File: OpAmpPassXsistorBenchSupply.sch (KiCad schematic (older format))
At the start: 32 parts

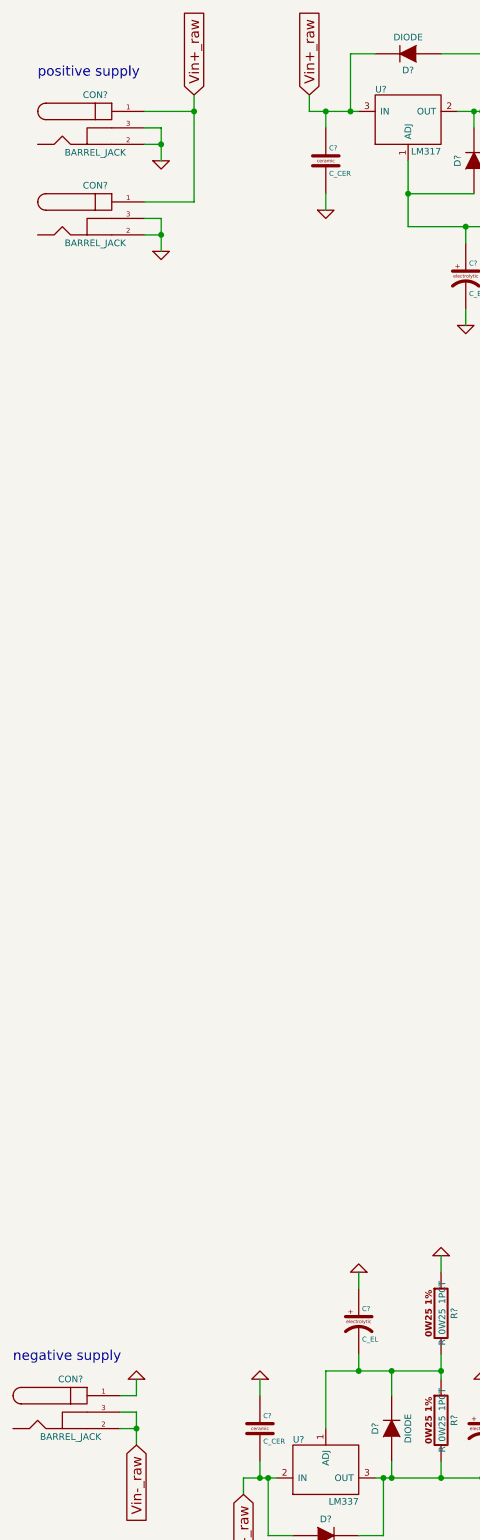
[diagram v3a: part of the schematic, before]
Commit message: adding input caps
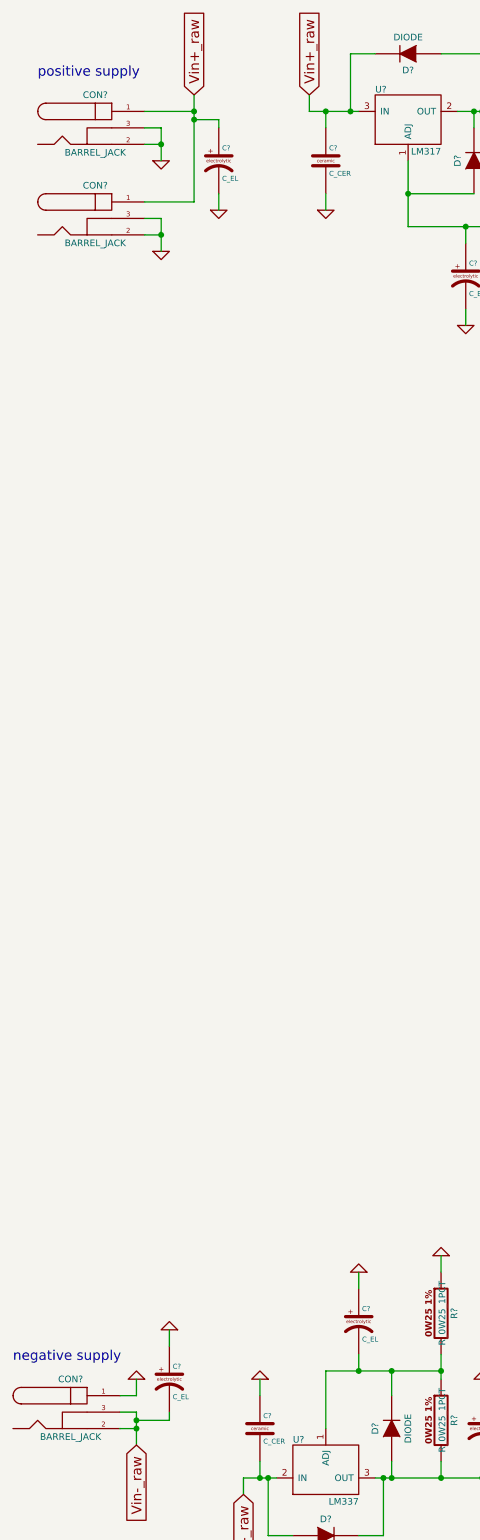
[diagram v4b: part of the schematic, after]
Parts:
- added C? (x2): C_EL, ~, symbol C_EL
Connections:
- net GND: now also C?.1, C?.2
- net Vin+_raw: now also C?.1
- net Vin-_raw: now also C?.2
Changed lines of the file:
@@
 Wire Wire Line
 	9750 8000 9950 8000
+$Comp
+L C_EL C?
+U 1 1 53366AD7
+P 2050 1700
+F 0 "C?" H 2070 1760 30  0000 L BNN
+F 1 "C_EL" H 2070 1610 30  0000 L TNN
+F 2 "~" H 2088 1550 30  0000 C CNN
+F 3 "~" H 2050 1700 60  0000 C CNN
+	1    2050 1700
+	1    0    0    -1
+$EndComp
+Wire Wire Line
+	1900 1450 2050 1450
+Wire Wire Line
+	2050 1450 2050 1500
+Connection ~ 1900 1450
+$Comp
+L GND #PWR?
+U 1 1 53366B79
+P 2050 2000
+F 0 "#PWR?" H 2050 2000 30  0001 C CNN
+F 1 "GND" H 2050 1930 30  0001 C CNN
+F 2 "" H 2050 2000 60  0000 C CNN
+F 3 "" H 2050 2000 60  0000 C CNN
+	1    2050 2000
+	1    0    0    -1
+$EndComp
+Wire Wire Line
+	2050 1900 2050 2000
+$Comp
+L C_EL C?
+U 1 1 53366C10
+P 1750 9100
+F 0 "C?" H 1770 9160 30  0000 L BNN
+F 1 "C_EL" H 1770 9010 30  0000 L TNN
+F 2 "~" H 1788 8950 30  0000 C CNN
+F 3 "~" H 1750 9100 60  0000 C CNN
+	1    1750 9100
+	1    0    0    -1
+$EndComp
+Wire Wire Line
+	1550 9350 1750 9350
+Wire Wire Line
+	1750 9350 1750 9300
+Connection ~ 1550 9350
+$Comp
+L GND #PWR?
+U 1 1 53366CB2
+P 1750 8800
+F 0 "#PWR?" H 1750 8800 30  0001 C CNN
+F 1 "GND" H 1750 8730 30  0001 C CNN
+F 2 "" H 1750 8800 60  0000 C CNN
+F 3 "" H 1750 8800 60  0000 C CNN
+	1    1750 8800
+	-1   0    0    1
+$EndComp
+Wire Wire Line
+	1750 8900 1750 8800
 $EndSCHEMATC

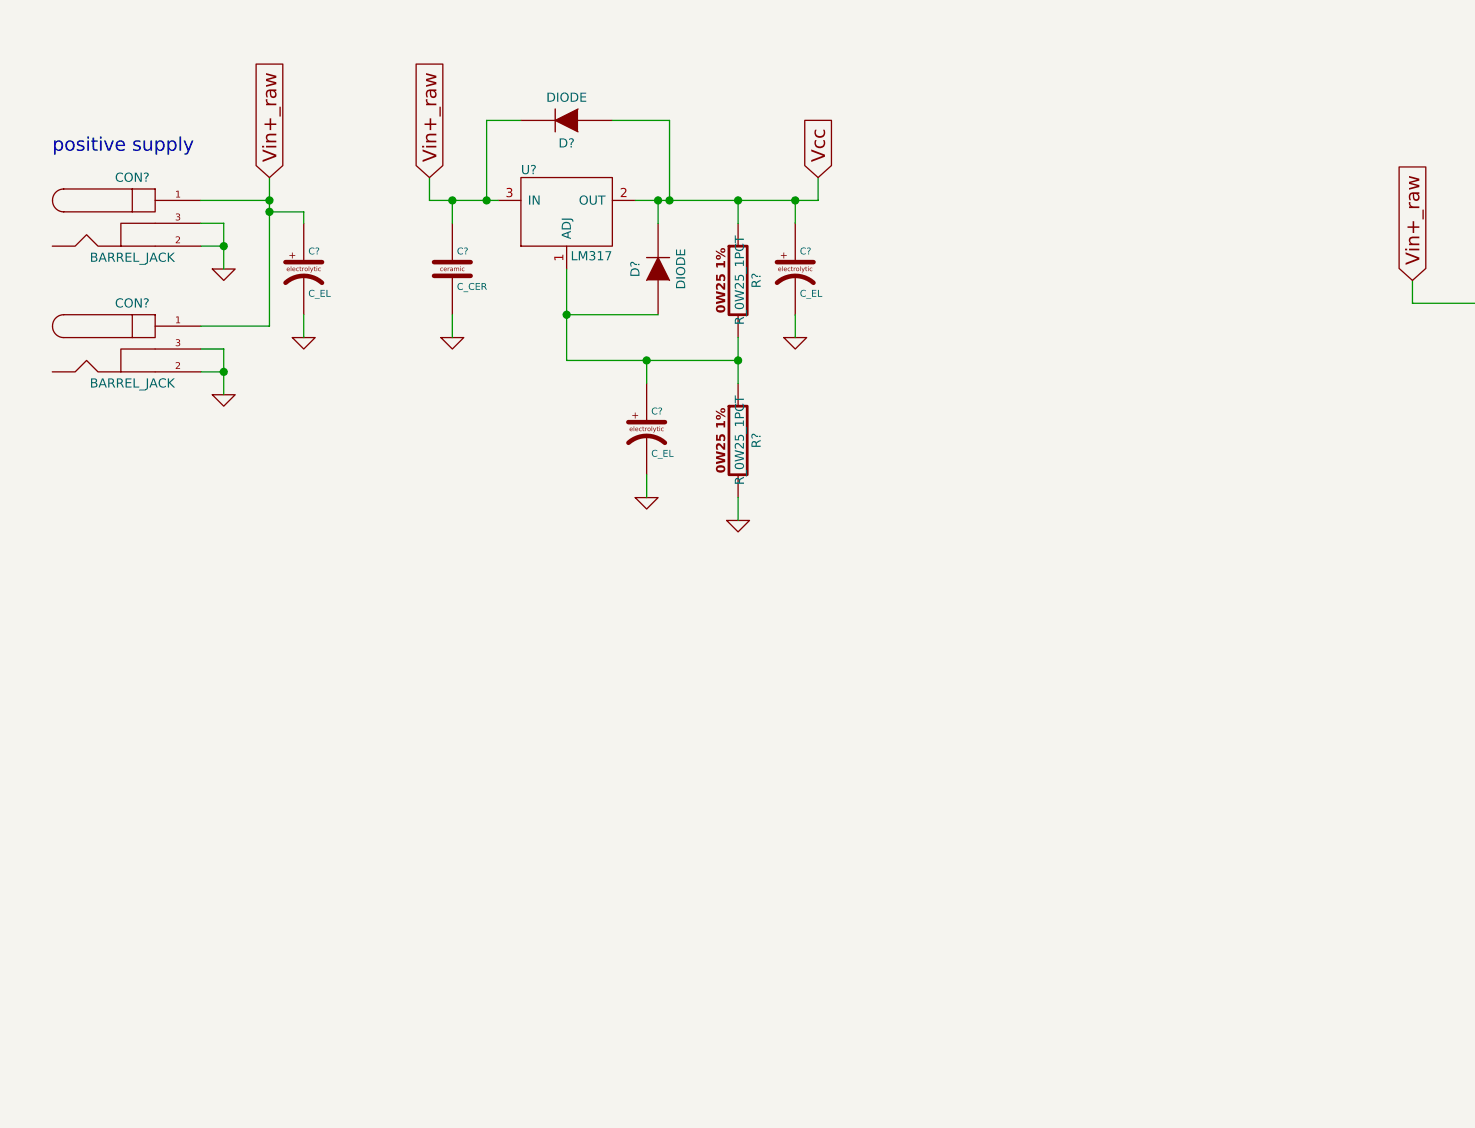
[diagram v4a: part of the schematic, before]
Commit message: adding input filter
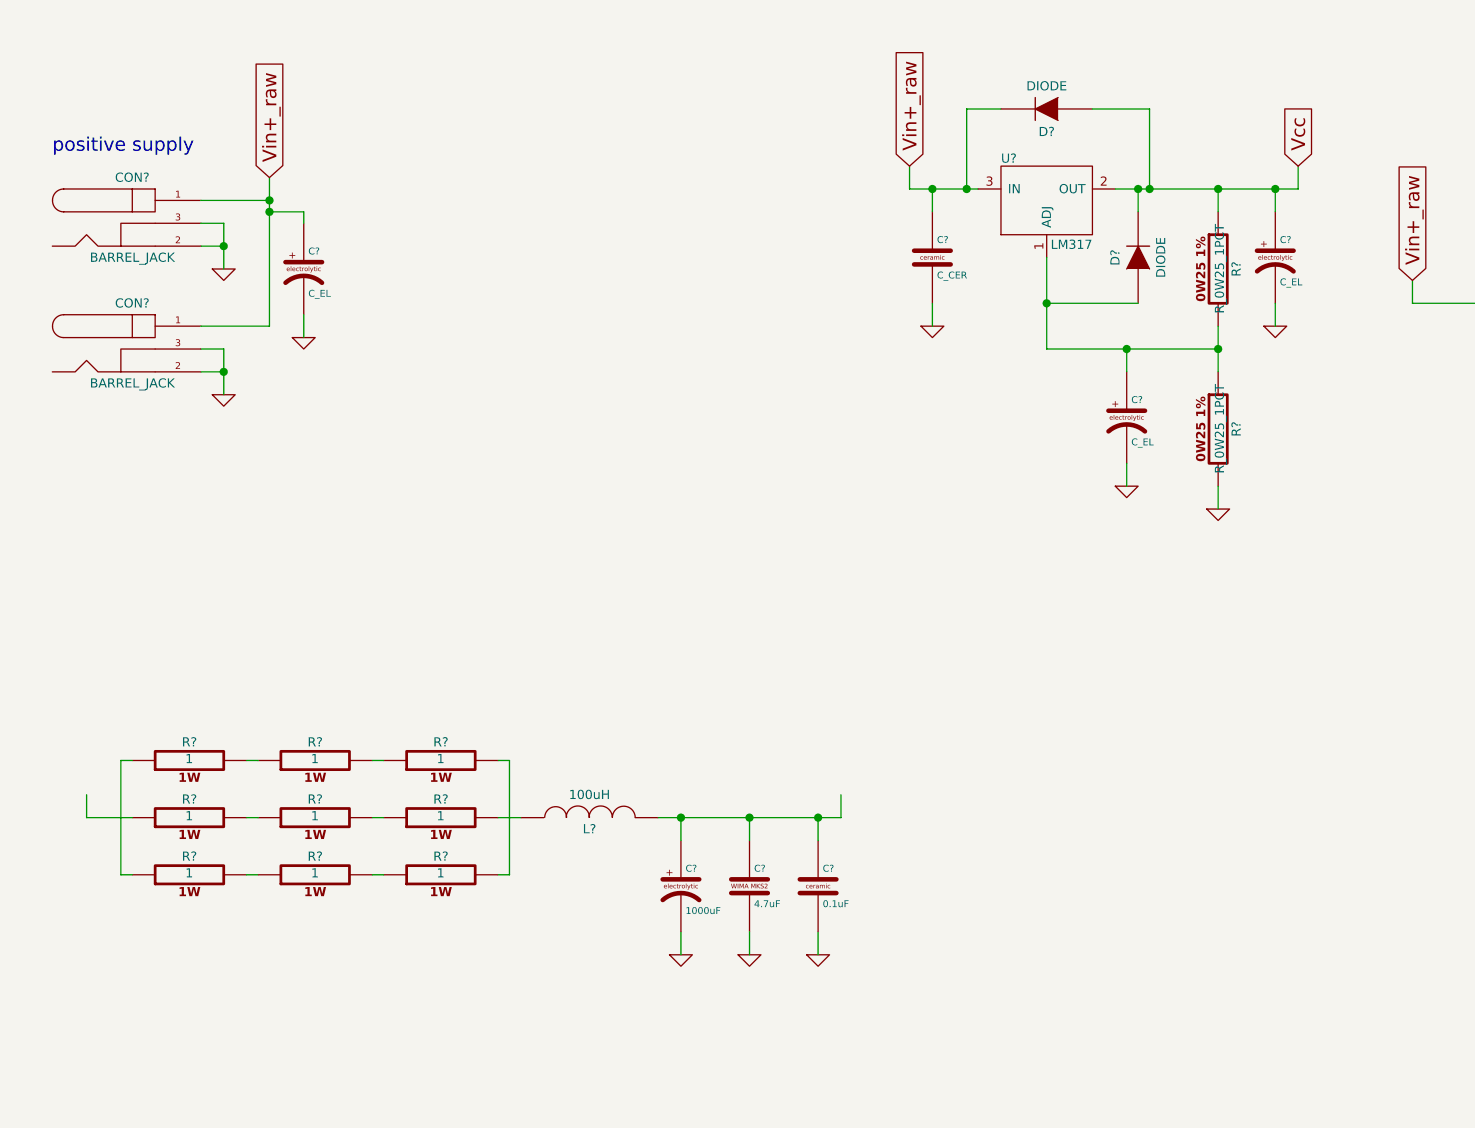
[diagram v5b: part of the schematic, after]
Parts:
- added C?: 1000uF, ~, symbol C_EL
- added C?: 4.7uF, ~, symbol C_MKS2
- added C?: 0.1uF, ~, symbol C_CER
- added L?: 100uH, ~, symbol INDUCTOR
- added R? (x9): 1, ~, symbol R_1W
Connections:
- net GND: now also C?.2, C?.2, C?.2
- new net: L?.1, R?.2
- new net: C?.1, C?.1, C?.1, L?.2
- new net: R?.1, R?.2 (x6)
- new net: R?.2, R?.2
- new net: R?.1, R?.1
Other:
- moved on the sheet: C?, D?, R?, U?

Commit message: working on input filter
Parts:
- removed C? (x2): C_EL, ~, symbol C_EL
- added C?: 1000uF, ~, symbol C_EL
- added C?: 4.7uF, ~, symbol C_MKS2
- added C?: 0.1uF, ~, symbol C_CER
- added L?: 100uH, ~, symbol INDUCTOR
- added R? (x9): 1, ~, symbol R_1W
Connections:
- net GND: now also C?.1, C?.1, C?.1
- new net: L?.1, R?.2
- new net: C?.2, C?.2, C?.2, L?.2
- new net: R?.1, R?.2 (x6)
- new net: R?.2, R?.2
- new net: R?.1, R?.1
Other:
- moved on the sheet: C?, D?, L?, R?, U?

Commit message: specifying regulator passive values
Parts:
- removed C?: 1000uF, ~, symbol C_EL
- removed C?: 4.7uF, ~, symbol C_MKS2
- removed C?: 0.1uF, ~, symbol C_CER
- removed L?: 100uH, ~, symbol INDUCTOR
- removed R? (x18): 1, ~, symbol R_1W
- added C? (x3): 1000uF, ~, symbol C_EL
- added C? (x3): 4.7uF, ~, symbol C_MKS2
- added C? (x3): 0.1uF, ~, symbol C_CER
- added L?: 100uH, ~, symbol INDUCTOR
- added R? (x2): 1, ~, symbol R_0W25
- added R? (x8): 1, ~, symbol R_0W5
- C? (x2): value C_CER -> 0.1uF
- C? (x4): value C_EL -> 10uF
- CON?: value BARREL_JACK -> 2.5x5.5mm
- CON? (x2): value BARREL_JACK -> 2.1x5.5mm
- D? (x4): value DIODE -> 1N4148
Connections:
- net GND: now also C?.1, C?.1, C?.1, C?.1, C?.1, C?.1, C?.2, C?.2, C?.2
- net at L?.1: now also C?.1, C?.1, C?.1, R?.2, R?.2, R?.2, R?.2
- net Vcc_filt: now reaches C?.1, C?.1, C?.1, L?.2
- net Vcc_filt: now also C?.1, D?.2 (K), Q?.1 (E), Q?.3 (C), R?.1, U?.3 (IN)
- net Vcc renamed Vcc_reg
- net Vee renamed Vee_reg
- removed net Vin+_raw: C?.1, CON?.1, CON?.1, D?.2 (K), Q?.1 (E), Q?.3 (C), R?.1, U?.3 (IN)
- net Vin-_raw renamed Vee_filt
- net Vee_filt: now also C?.2, C?.2, C?.2, L?.2; no longer CON?.2, CON?.3
- new net: C?.2, C?.2, C?.2, L?.1, R?.2, R?.2
- new net: R?.1, R?.2 (x4)
- new net Vcc_raw: CON?.1, CON?.1, R?.1, R?.1, R?.1, R?.1
- new net Vee_raw: CON?.2, CON?.3, R?.1, R?.1
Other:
- note added: "0.5 Ohm, 0.5 Watt"
- note added: "0.5 Ohm, 4 Watt"
- moved on the sheet: C?, L?

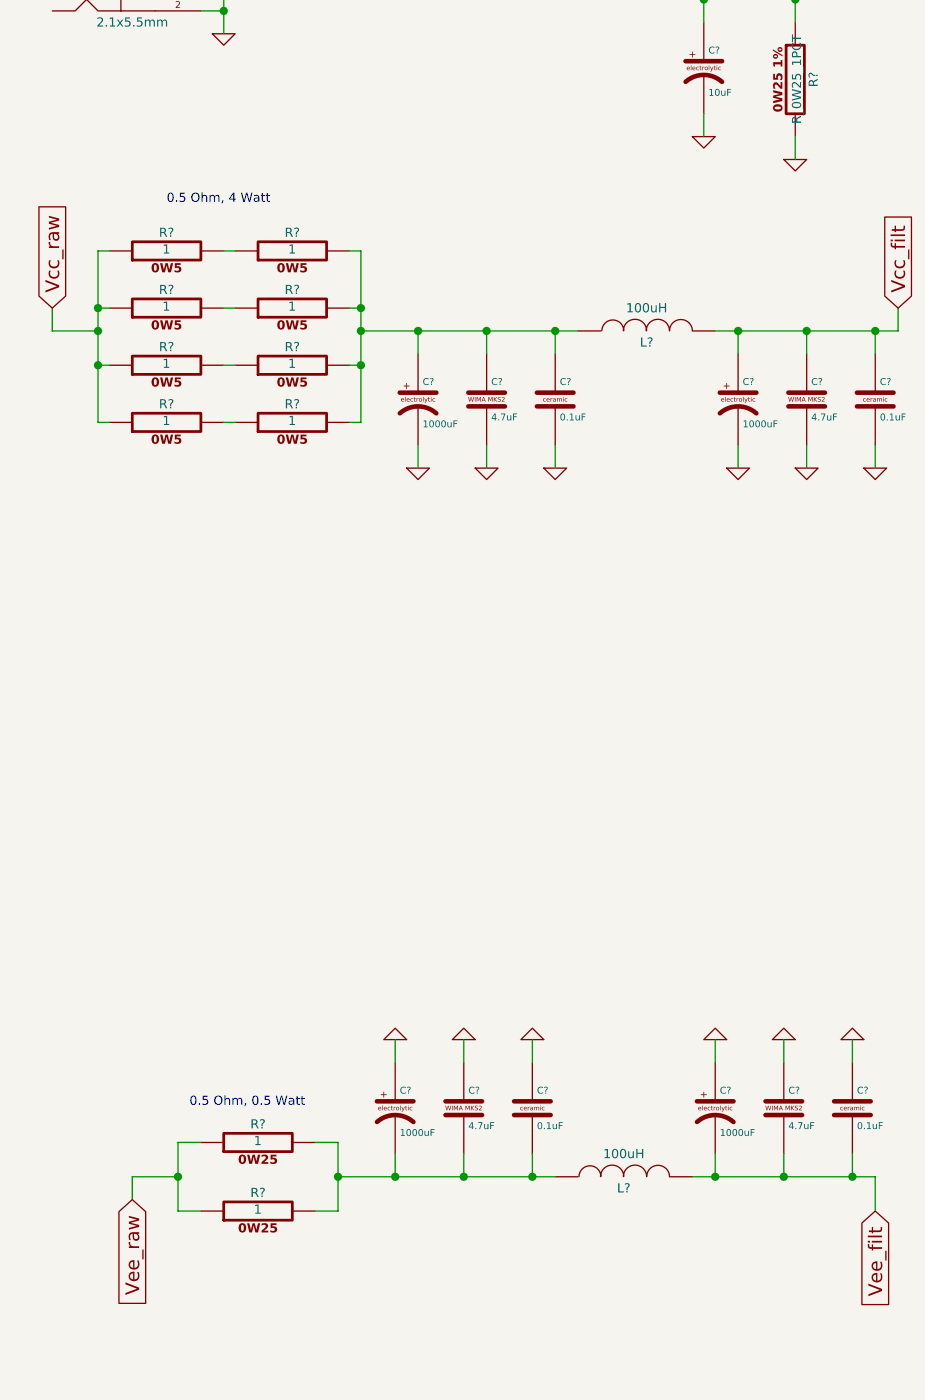
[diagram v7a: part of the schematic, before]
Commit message: tweaking filter values
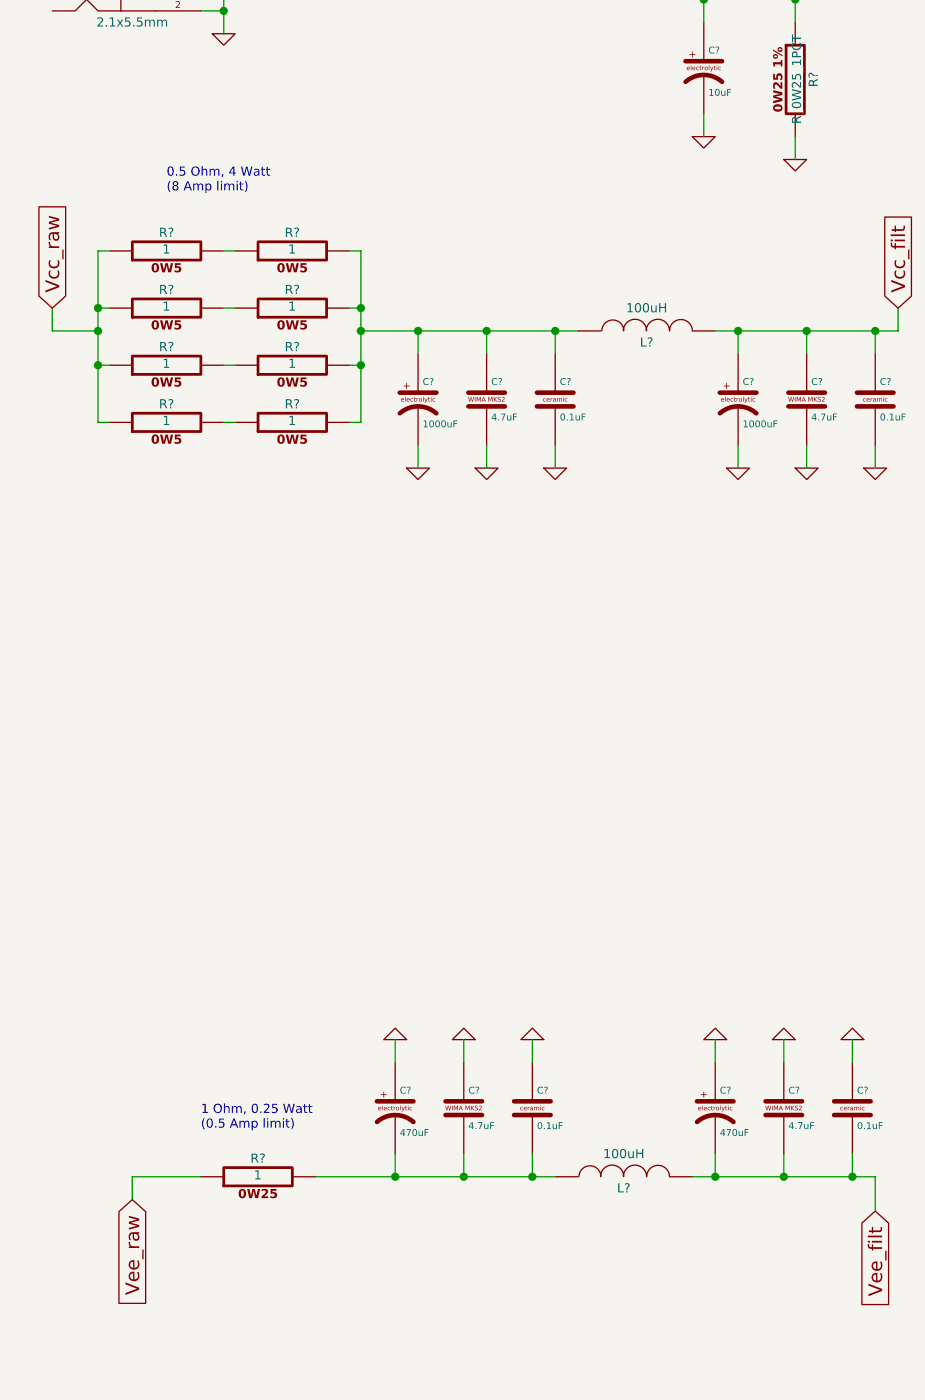
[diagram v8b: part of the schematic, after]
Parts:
- removed R?: 1, ~, symbol R_0W25
- C? (x2): value 1000uF -> 470uF
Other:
- note added: "0.5 Ohm, 4 Watt\n(8 Amp limit)"
- note added: "1 Ohm, 0.25 Watt\n(0.5 Amp limit)"
- note removed: "0.5 Ohm, 0.5 Watt"
- note removed: "0.5 Ohm, 4 Watt"
- moved on the sheet: R?
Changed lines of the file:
@@
 P 3850 6950
 F 0 "C?" H 3870 7010 30  0000 L BNN
-F 1 "1000uF" H 3870 6860 30  0000 L TNN
+F 1 "470uF" H 3870 6860 30  0000 L TNN
 F 2 "~" H 3888 6800 30  0000 C CNN
 F 3 "~" H 3850 6950 60  0000 C CNN
@@
 $EndComp
 Wire Wire Line
-	2200 7250 3150 7250
-Wire Wire Line
-	1500 7250 1300 7250
-Connection ~ 1500 7250
+	2100 7250 3150 7250
+Wire Wire Line
+	1300 7250 1600 7250
 $Comp
 L C_EL C?
@@
 P 2450 6950
 F 0 "C?" H 2470 7010 30  0000 L BNN
-F 1 "1000uF" H 2470 6860 30  0000 L TNN
+F 1 "470uF" H 2470 6860 30  0000 L TNN
 F 2 "~" H 2488 6800 30  0000 C CNN
 F 3 "~" H 2450 6950 60  0000 C CNN
@@
 L R_0W25 R?
 U 1 1 53374617
-P 1850 7100
-F 0 "R?" V 1930 7100 40  0000 C CNN
-F 1 "1" V 1857 7101 40  0000 C CNN
-F 2 "~" V 1780 7100 30  0000 C CNN
-F 3 "~" H 1850 7100 30  0000 C CNN
-	1    1850 7100
-	0    -1   -1   0
-$EndComp
-$Comp
-L R_0W25 R?
-U 1 1 53374638
-P 1850 7400
-F 0 "R?" V 1930 7400 40  0000 C CNN
-F 1 "1" V 1857 7401 40  0000 C CNN
-F 2 "~" V 1780 7400 30  0000 C CNN
-F 3 "~" H 1850 7400 30  0000 C CNN
-	1    1850 7400
-	0    -1   -1   0
-$EndComp
-Wire Wire Line
-	1600 7100 1500 7100
-Wire Wire Line
-	1500 7100 1500 7400
-Wire Wire Line
-	1500 7400 1600 7400
-Wire Wire Line
-	2100 7100 2200 7100
-Wire Wire Line
-	2200 7100 2200 7400
-Wire Wire Line
-	2200 7400 2100 7400
-Connection ~ 2200 7250
+P 1850 7250
+F 0 "R?" V 1930 7250 40  0000 C CNN
+F 1 "1" V 1857 7251 40  0000 C CNN
+F 2 "~" V 1780 7250 30  0000 C CNN
+F 3 "~" H 1850 7250 30  0000 C CNN
+	1    1850 7250
+	0    -1   -1   0
+$EndComp
 $Comp
 L R_0W5 R?
@@
 Text GLabel 6900 1750 1    60   Input ~ 0
 Vcc_filt
-Text Notes 1550 6950 0    40   ~ 0
-0.5 Ohm, 0.5 Watt
-Text Notes 1450 3000 0    40   ~ 0
-0.5 Ohm, 4 Watt
+Text Notes 1600 7050 0    40   ~ 0
+1 Ohm, 0.25 Watt\n(0.5 Amp limit)
+Text Notes 1450 2950 0    40   ~ 0
+0.5 Ohm, 4 Watt\n(8 Amp limit)
 $EndSCHEMATC
